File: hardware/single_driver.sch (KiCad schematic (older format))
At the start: 41 parts, among them IC1 TMC5161

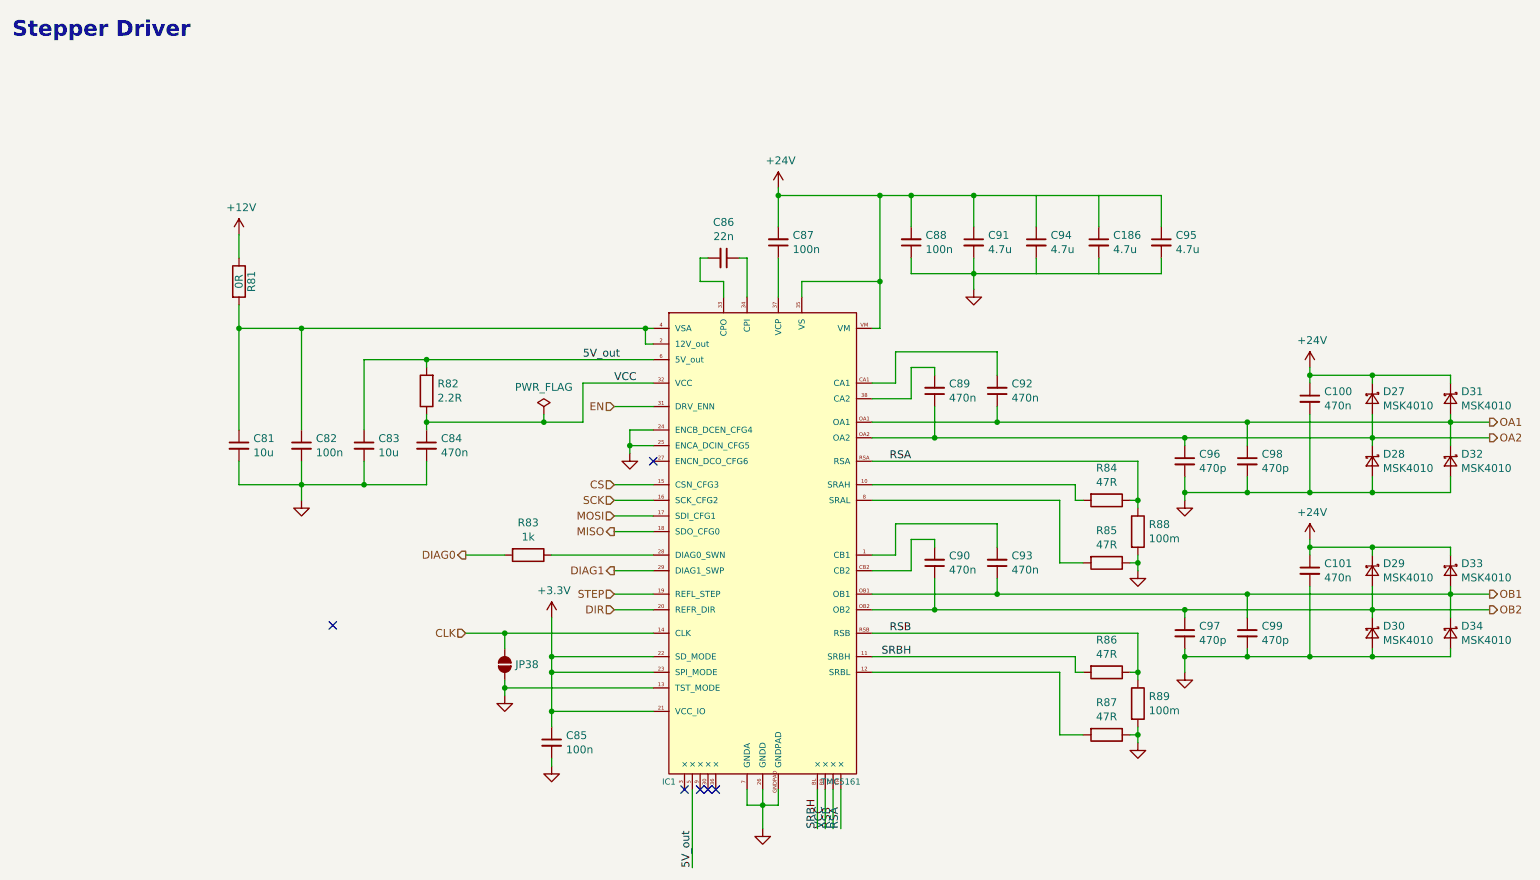
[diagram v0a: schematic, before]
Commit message: replaced stepper driver
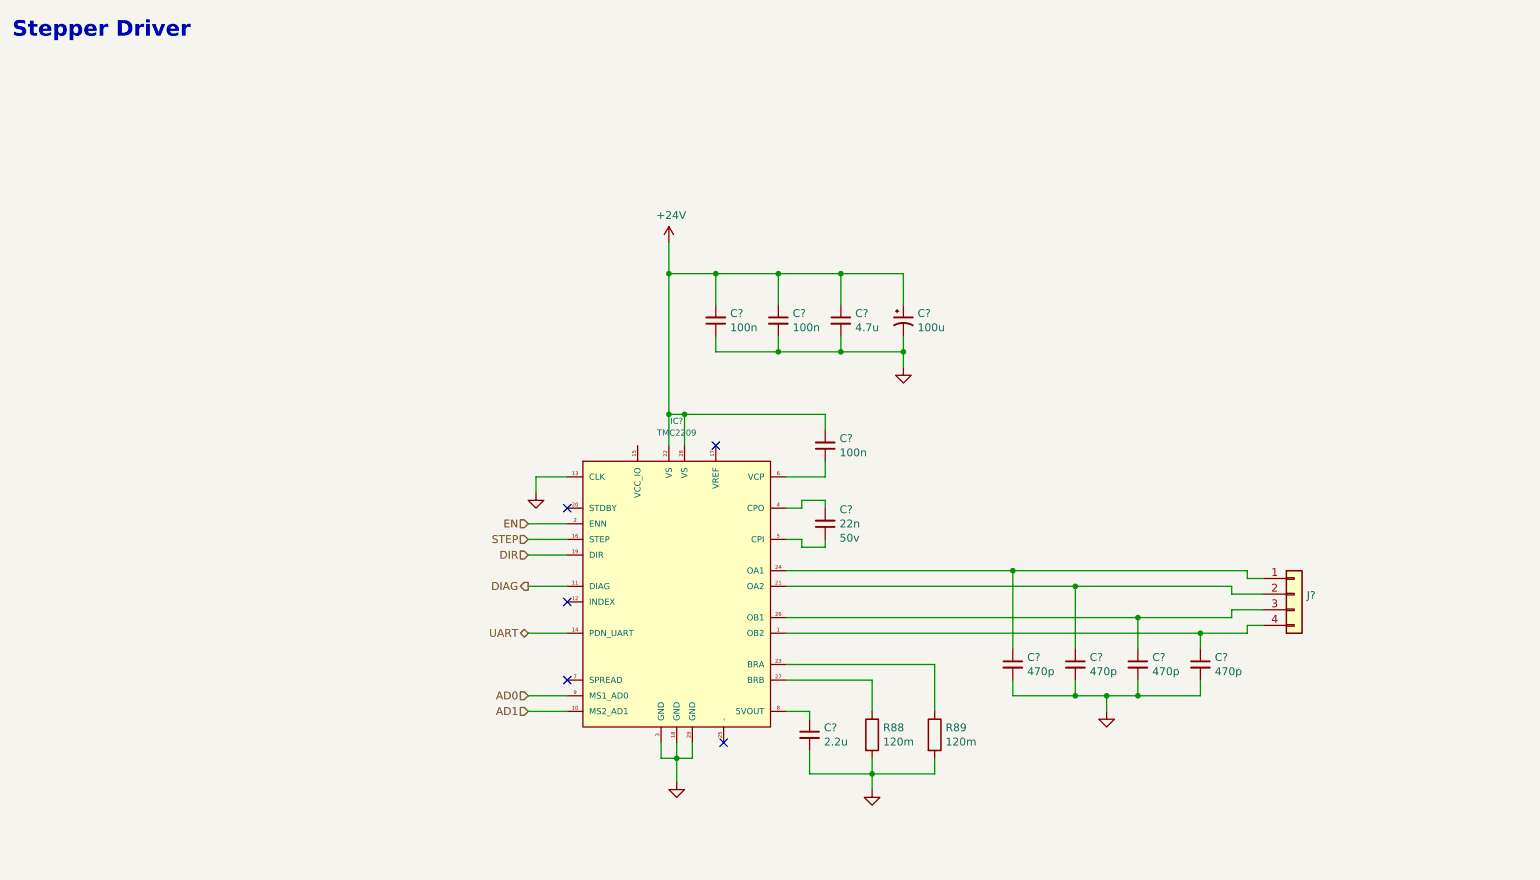
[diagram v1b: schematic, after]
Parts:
- removed C100, C101, C84, C89, C90, C92, C93: 470n, _Generic:0603_CAP, symbol Device:C_Small
- removed C186, C95: 4.7u, _Generic:1210_CAP, symbol Device:C_Small
- removed C81, C83: 10u, _Generic:0603_CAP, symbol Device:C_Small
- removed C82, C85: 100n, _Generic:0603_CAP, symbol Device:C_Small
- removed D27, D28, D29, D30, D31, D32, D33, D34: MSK4010, _Generic:SOD-523_DIODE, symbol Device:D_Schottky_Small
- removed IC1: TMC5161, footprints:QFN42L, symbol #Driver_Motor:TMC5161
- removed JP38: SolderJumper_2_Open, _Generic:Solder Jumper 2P, symbol #PCB_Only:SolderJumper_2_Open
- removed R81: 0R, _Generic:0603_RES, symbol Device:R
- removed R82: 2.2R, _Generic:0603_RES, symbol Device:R
- removed R83: 1k, _Generic:0603_RES, symbol Device:R
- removed R84, R85, R86, R87: 47R, _Generic:0603_RES, symbol Device:R
- added C?: 2.2u, _Generic:0603_CAP, symbol Device:C_Small
- added C?: 100u, symbol Device:CP1_Small
- added IC?: TMC2209, TMC5161:QFN42L, symbol #Driver_Motor:TMC2209
- added J?: Conn_01x04, _Generic:JST_XH_4P, symbol Connector_Generic:Conn_01x04
- C86: Voltage (none) -> 50v
- C91: value 4.7u -> 100n
- R88, R89: value 100m -> 120m
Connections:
- net +24V: now also C?.1, IC?.22 (VS), IC?.28 (VS)
- net DIR: now also IC?.19 (DIR)
- net EN: now also IC?.2 (ENN)
- net GND: now also C?.2, C?.2, IC?.13 (CLK), IC?.18 (GND), IC?.29 (GND), IC?.3 (GND)
- net STEP: now also IC?.16 (STEP)
- net at C86.2: now also IC?.4 (CPO)
- net at C86.1: now also IC?.5 (CPI)
- net at C87.1: now also IC?.6 (VCP)
- net OA1: no longer names the net of C98.1
- net OA1: now also IC?.21 (OA2), J?.2 (Pin_2)
- net OA2: no longer names the net of C96.1
- net OA2: now also IC?.24 (OA1), J?.1 (Pin_1)
- net OB1: no longer names the net of C99.1
- net OB1: now also IC?.1 (OB2), J?.4 (Pin_4)
- net OB2: no longer names the net of C97.1
- net OB2: now also IC?.26 (OB1), J?.3 (Pin_3)
- net RSA: no longer names the net of R88.1
- net RSA: now also IC?.27 (BRB)
- net RSB: no longer names the net of R89.1
- net RSB: now also IC?.23 (BRA)
- new net: C?.1, IC?.8 (5VOUT)
- new net AD0: IC?.9 (MS1_AD0)
- new net AD1: IC?.10 (MS2_AD1)
- new net DIAG: IC?.11 (DIAG)
- new net UART: IC?.14 (PDN_UART)
- no-connect marks 6 -> 5
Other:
- moved on the sheet: C?, R88, R89

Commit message: layout
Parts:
- added C119: 100n, _Generic:0603_CAP, symbol Device:C_Small
- added C126, C127: 4.7u, _Generic:1210_CAP, symbol Device:C_Small
- C111: renamed from C?; footprint (none) -> Capacitor_SMD:CP_Elec_6.3x7.7
- C91: value 100n -> 4.7u
- IC4: renamed from IC?; footprint TMC5161:QFN42L -> Package_DFN_QFN:QFN-28-1EP_5x5mm_P0.5mm_EP3.35x3.35mm
- gave numbers to parts that had none: 2
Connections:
- net +24V: now also C119.2, C126.1, C127.1
- net GND: now also C119.1, C126.2, C127.2
- net at C96.1, IC4.24 (OA1): now also J10.3 (Pin_3); no longer J10.1 (Pin_1)
- net at C98.1, IC4.21 (OA2): now also J10.4 (Pin_4); no longer J10.2 (Pin_2)
- net at C97.1, IC4.26 (OB1): now also J10.2 (Pin_2); no longer J10.3 (Pin_3)
- net at C99.1, IC4.1 (OB2): now also J10.1 (Pin_1); no longer J10.4 (Pin_4)

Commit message: routing
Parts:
- removed C111: 100u, Capacitor_SMD:CP_Elec_6.3x7.7, symbol Device:CP1_Small
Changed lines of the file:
@@
 $Descr A4 11693 8268
 encoding utf-8
-Sheet 8 19
+Sheet 7 19
 Title "Kajikia - Stepper Driver"
 Date "2019-01-23"
@@
 	5850 2750 6050 2750
 Wire Wire Line
-	6250 2750 6250 2650
-Wire Wire Line
-	6250 2450 6250 2250
-Wire Wire Line
 	3850 3850 4100 3850
 Wire Wire Line
@@
 	1    0    0    -1
 $EndComp
-Wire Wire Line
-	6250 2250 6050 2250
 Connection ~ 4750 2250
 Wire Wire Line
@@
 Wire Wire Line
 	5850 2250 5650 2250
-Connection ~ 6250 2750
-$Comp
-L Device:CP1_Small C?
-U 1 1 5D86695A
-P 6250 2550
-AR Path="/60C2EDFB/60ECA8FF/5D86695A" Ref="C?"  Part="1"
-AR Path="/60C2EDFB/5B411670/5D86695A" Ref="C?"  Part="1"
-AR Path="/60C2EDFB/60ECD6D9/5D86695A" Ref="C?"  Part="1"
-AR Path="/60C2EDFB/60ED586F/5D86695A" Ref="C?"  Part="1"
-AR Path="/60C2EDFB/60ED8641/5D86695A" Ref="C?"  Part="1"
-AR Path="/5D8A86C3/5D86695A" Ref="C111"  Part="1"
-AR Path="/5D8C6DBC/5D86695A" Ref="C53"  Part="1"
-AR Path="/5D8E4767/5D86695A" Ref="C89"  Part="1"
-AR Path="/5D90218A/5D86695A" Ref="C100"  Part="1"
-F 0 "C111" H 6341 2596 50  0000 L CNN
-F 1 "100u" H 6341 2505 50  0000 L CNN
-F 2 "Capacitor_SMD:CP_Elec_6.3x7.7" H 6250 2550 50  0001 C CNN
-F 3 "~" H 6250 2550 50  0001 C CNN
-	1    6250 2550
-	1    0    0    -1
-$EndComp
 Connection ~ 7750 4450
 Connection ~ 8150 4550
@@
 Wire Wire Line
 	6050 2750 6250 2750
-Connection ~ 6050 2250
 Wire Wire Line
 	6050 2250 5850 2250

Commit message: pcb v1
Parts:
- added C79: 100n, _Generic:0603_CAP, symbol Device:C_Small
- C107: value 2.2u -> 10u
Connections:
- net AD0 is gone; now on net GND: IC4.9 (MS1_AD0)
- net AD1 is gone; now on net GND: IC4.10 (MS2_AD1)
- net EN is gone; now on net GND: IC4.2 (ENN)
- net GND: now also IC4.20 (STDBY), IC4.7 (SPREAD), C79.1
- net +3V3: now reaches IC4.15 (VCC_IO)
- net +3V3: now also C79.2
- no-connect marks 5 -> 3
